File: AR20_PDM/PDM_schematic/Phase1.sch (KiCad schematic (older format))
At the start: 19 parts, among them Q1 BTS50025-1TAD, U1 INA233

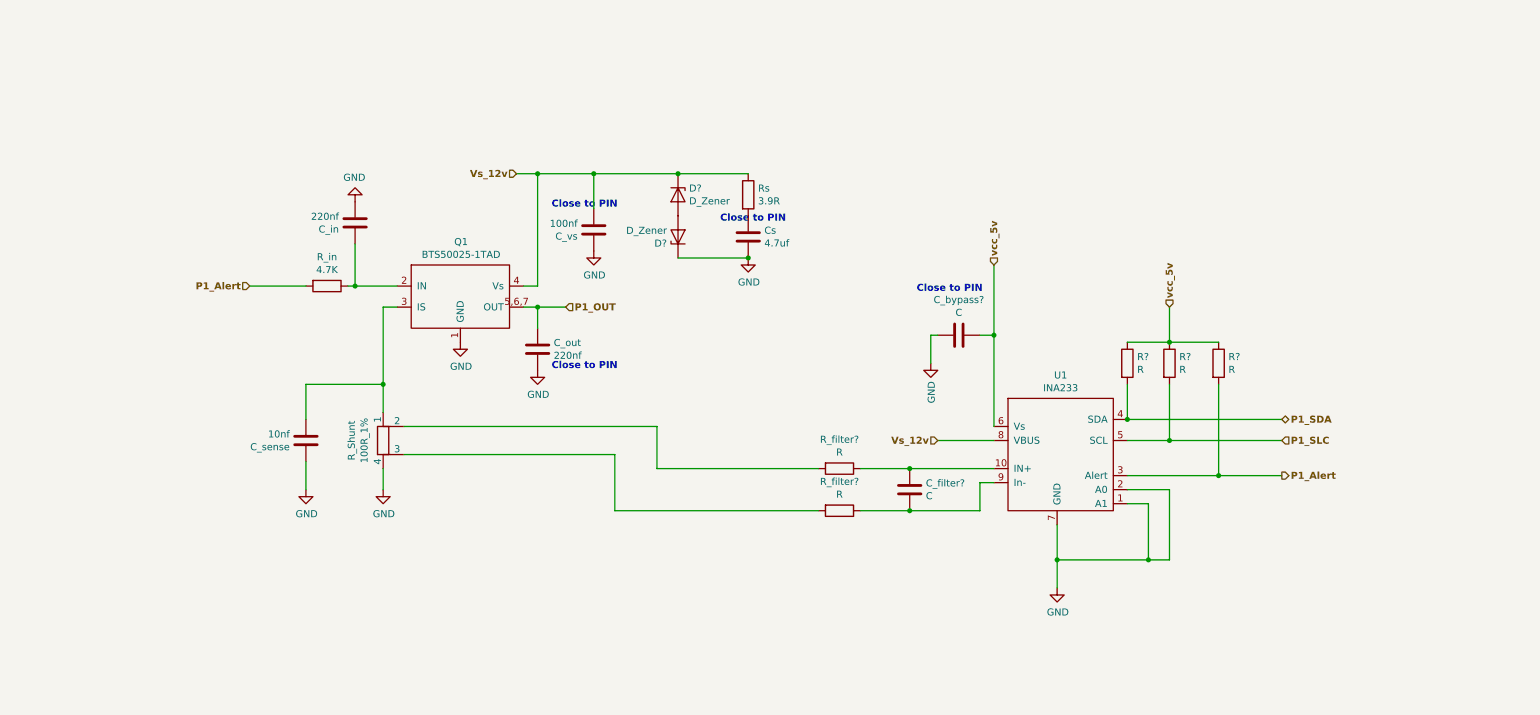
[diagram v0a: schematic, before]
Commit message: Refining pdm schematics
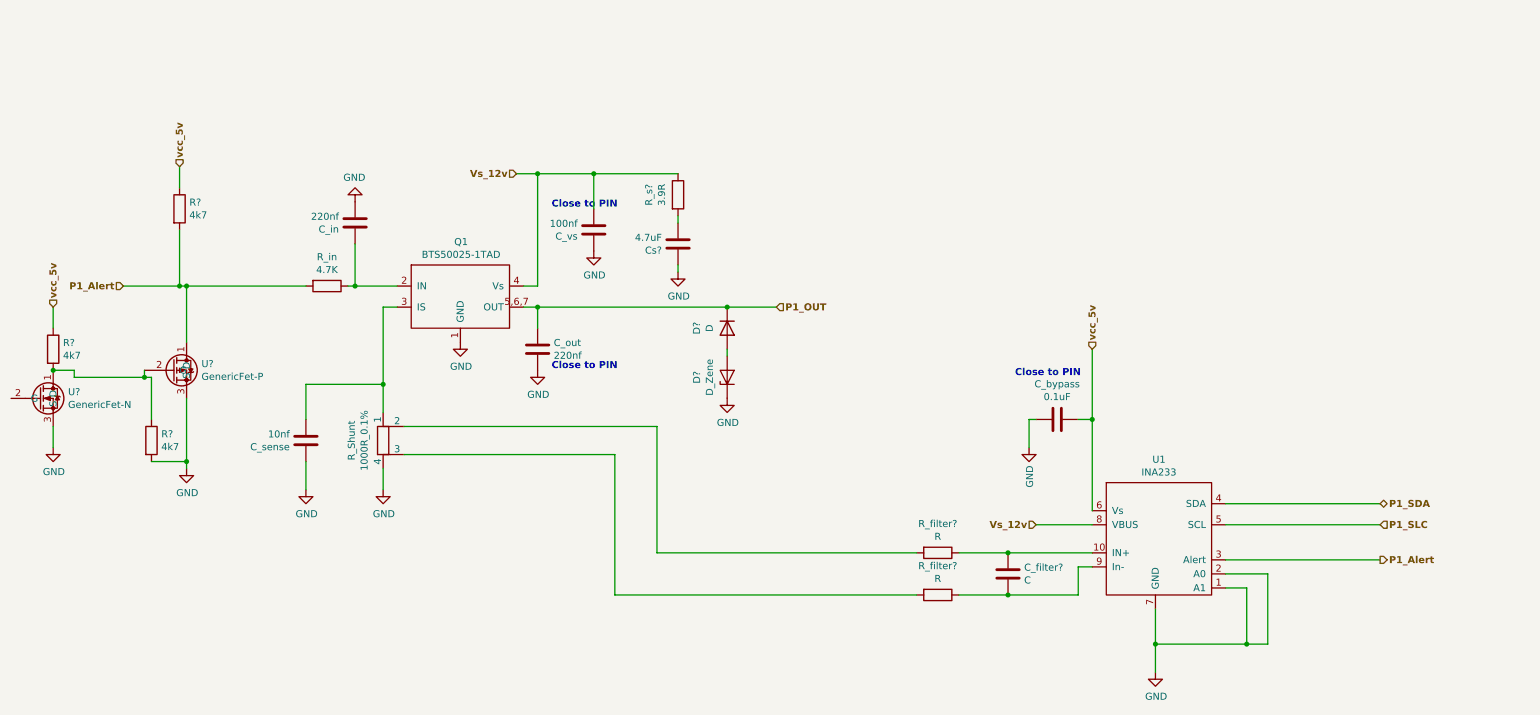
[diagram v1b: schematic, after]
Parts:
- removed Cs: 4.7uf, symbol AR20_PDM_v1-rescue:C-Device
- removed D? (x2): D_Zener, symbol AR20_PDM_v1-rescue:D_Zener-Device
- removed R? (x2): R, symbol AR20_PDM_v1-rescue:R-Device
- removed Rs: 3.9R, symbol AR20_PDM_v1-rescue:R-Device
- added Cs?: 4.7uF, symbol AR20_PDM_v1-rescue:C-Device
- added D?: D_Zene, symbol AR20_PDM_v1-rescue:D_Zener-Device
- added D?: D, symbol AR20_PDM_v1-rescue:DIODE-Simulation_SPICE
- added R? (x2): 4k7, symbol AR20_PDM_v1-rescue:R-Device
- added R_s?: 3.9R, symbol AR20_PDM_v1-rescue:R-Device
- added U?: GenericFet-P, symbol AR20_PDM_v1-rescue:GenericFet-P
- added U?: GenericFet-N, symbol AR20_PDM_v1-rescue:GenericFet-N
- C_bypass: renamed from C_bypass?; value C -> 0.1uF
- R?: value R -> 4k7
- R_Shunt: value 100R_1% -> 1000R_0.1%
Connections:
- net GND: now also Cs?.1, D?.1 (K), R?.2, U?.3 (S), U?.3 (S)
- net P1_Alert: now also U?.1 (D)
- net P1_OUT: now also D?.2 (K)
- net Vs_12v: now also R_s?.1
- net vcc_5v: now also R?.1
- new net: D?.1 (A), D?.2 (A)
- new net: Cs?.2, R_s?.2
- new net: R?.1, R?.2, U?.1 (D), U?.2 (G)
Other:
- moved on the sheet: C_bypass, C_filter?, R?, R_filter?, U1

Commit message: Refining pdm phase 1
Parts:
- removed R?: 4k7, symbol AR20_PDM_v1-rescue:R-Device
- removed U?: GenericFet-P, symbol AR20_PDM_v1-rescue:GenericFet-P
- removed U?: GenericFet-N, symbol AR20_PDM_v1-rescue:GenericFet-N
- added R?: 4k7, symbol AR20_PDM_v1-rescue:R-Device
- added U? (x2): Fet-P, symbol AR20_PDM_v1-rescue:GenericFet-P
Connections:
- net GND: now also R?.2, U?.3 (S), U?.3 (S)
- net P1_Alert: now also U?.1 (D), U?.1 (D)
- net P1_EN: now reaches R?.1
- net P1_EN: now also U?.2 (G)
- new net P1_mcu_EN: R?.1, U?.2 (G)
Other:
- moved on the sheet: C_bypass, C_filter?, C_in, C_out, C_sense, C_vs, Cs?, D?, Q1, R?, R_Shunt, R_filter?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

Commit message: PDM Phase 1 mostly complete
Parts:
- removed C_filter?: C, symbol AR20_PDM_v1-rescue:C-Device
- removed R_filter? (x2): R, symbol AR20_PDM_v1-rescue:R-Device
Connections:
- net at U1.10 (IN+): now also R_Shunt.2
- net at U1.9 (In-): now also R_Shunt.3
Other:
- note added: "Configurable address, \nmust be different for each chip"
- moved on the sheet: R?, U?
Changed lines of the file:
@@
-$EndComp
-$Comp
-L AR20_PDM_v1-rescue:C-Device C_filter?
-U 1 1 5DAAC1F5
-P 8150 4450
-F 0 "C_filter?" H 8265 4496 50  0000 L CNN
-F 1 "C" H 8265 4405 50  0000 L CNN
-F 2 "" H 8188 4300 50  0001 C CNN
-F 3 "~" H 8150 4450 50  0001 C CNN
-	1    8150 4450
-	1    0    0    -1
 $EndComp
 $Comp
@@
 Wire Wire Line
 	4800 2550 4800 2700
-Wire Wire Line
-	9200 4700 9200 4950
-Wire Wire Line
-	8750 4300 8150 4300
-Connection ~ 8150 4300
 $Comp
 L AR20_PDM_v1-rescue:GND-power #PWR?
@@
 	3700 3850 3700 3700
 Wire Wire Line
-	8150 4600 7800 4600
-Wire Wire Line
-	7800 4300 8150 4300
-Wire Wire Line
 	8750 2850 8750 3350
 Wire Wire Line
@@
 Wire Wire Line
 	9700 4450 10000 4450
-Wire Wire Line
-	10000 4450 10000 4950
 $Comp
 L AR20_PDM_v1-rescue:GND-power #PWR?
@@
 Wire Wire Line
 	3500 2400 3800 2400
-Wire Wire Line
-	9850 4950 9200 4950
-Connection ~ 9200 4950
-Wire Wire Line
-	9200 4950 9200 5150
-Wire Wire Line
-	9850 4950 10000 4950
-Connection ~ 9850 4950
 $Comp
 L AR20_PDM_v1-rescue:BTS50025-1TAD Q1
@@
 	3850 3600 5350 3600
 Wire Wire Line
-	3850 3400 5650 3400
+	3850 3400 5450 3400
 Text HLabel 2250 1550 1    50   Input ~ 10
 vcc_5v
-Wire Wire Line
-	8750 4400 8650 4400
-Wire Wire Line
-	8650 4400 8650 4600
-Wire Wire Line
-	8650 4600 8150 4600
-Connection ~ 8150 4600
 Wire Wire Line
 	9700 4100 10350 4100
@@
 Connection ~ 5200 1600
 Wire Wire Line
-	5650 3400 5650 4300
-Wire Wire Line
-	5650 4300 7500 4300
-$Comp
-L AR20_PDM_v1-rescue:R-Device R_filter?
-U 1 1 5DAAC263
-P 7650 4600
-F 0 "R_filter?" V 7443 4600 50  0000 C CNN
-F 1 "R" V 7534 4600 50  0000 C CNN
-F 2 "" V 7580 4600 50  0001 C CNN
-F 3 "~" H 7650 4600 50  0001 C CNN
-	1    7650 4600
-	0    1    1    0
-$EndComp
-$Comp
-L AR20_PDM_v1-rescue:R-Device R_filter?
-U 1 1 5DAAC1FB
-P 7650 4300
-F 0 "R_filter?" V 7443 4300 50  0000 C CNN
-F 1 "R" V 7534 4300 50  0000 C CNN
-F 2 "" V 7580 4300 50  0001 C CNN
-F 3 "~" H 7650 4300 50  0001 C CNN
-	1    7650 4300
-	0    1    1    0
-$EndComp
-Wire Wire Line
-	7500 4600 5350 4600
-Wire Wire Line
-	5350 3600 5350 4600
-Text HLabel 1250 1900 1    50   Input ~ 10
+	5450 3400 5450 4300
+Wire Wire Line
+	5350 3600 5350 4400
+Text HLabel 1350 1900 1    50   Input ~ 10
 P1_Alert
 Wire Wire Line
@@
 $Comp
 L AR20_PDM_v1-rescue:GND-power #PWR?
-U 1 1 5DC19763
-P 2500 3600
-F 0 "#PWR?" H 2500 3350 50  0001 C CNN
-F 1 "GND" H 2505 3427 50  0000 C CNN
-F 2 "" H 2500 3600 50  0001 C CNN
-F 3 "" H 2500 3600 50  0001 C CNN
-	1    2500 3600
-	1    0    0    -1
-$EndComp
-Wire Wire Line
-	2500 3200 2500 3550
-Connection ~ 2500 3550
-Wire Wire Line
-	2500 3550 2500 3600
+U 1 1 5DC2BC32
+P 1350 3600
+F 0 "#PWR?" H 1350 3350 50  0001 C CNN
+F 1 "GND" H 1355 3427 50  0000 C CNN
+F 2 "" H 1350 3600 50  0001 C CNN
+F 3 "" H 1350 3600 50  0001 C CNN
+	1    1350 3600
+	1    0    0    -1
+$EndComp
+Wire Wire Line
+	1350 3200 1350 3550
+Wire Wire Line
+	1000 3550 1350 3550
+Connection ~ 1350 3550
+Wire Wire Line
+	1350 3550 1350 3600
+Wire Wire Line
+	1350 2400 1350 2800
+$Comp
+L AR20_PDM_v1-rescue:R-Device R?
+U 1 1 5DC2BC49
+P 1000 3400
+F 0 "R?" H 1070 3446 50  0000 L CNN
+F 1 "4k7" H 1070 3355 50  0000 L CNN
+F 2 "" V 930 3400 50  0001 C CNN
+F 3 "~" H 1000 3400 50  0001 C CNN
+	1    1000 3400
+	1    0    0    -1
+$EndComp
+Wire Wire Line
+	1000 3250 1000 3000
+Wire Wire Line
+	1000 3000 1050 3000
+Wire Wire Line
+	1350 1900 1350 2400
+Connection ~ 1350 2400
+Wire Wire Line
+	1350 2400 2250 2400
+Wire Wire Line
+	2250 2400 2500 2400
+Connection ~ 2500 2400
+Wire Wire Line
+	2500 2400 3150 2400
+$Comp
+L AR20_PDM_v1-rescue:GenericFet-P U?
+U 1 1 5DC2BC43
+P 1350 2500
+F 0 "U?" H 1456 2046 50  0000 L CNN
+F 1 "Fet-P" H 1456 1955 50  0000 L CNN
+F 2 "" H 1350 2500 50  0001 C CNN
+F 3 "" H 1350 2500 50  0001 C CNN
+	1    1350 2500
+	1    0    0    -1
+$EndComp
+Connection ~ 1000 3000
+Text HLabel 700  3100 3    50   Input ~ 0
+P1_mcu_EN
+Wire Wire Line
+	700  3000 700  3100
+Wire Wire Line
+	700  3000 1000 3000
+Wire Wire Line
+	5450 4300 8750 4300
+Wire Wire Line
+	5350 4400 8750 4400
+Wire Wire Line
+	9200 4950 9200 5150
+Wire Wire Line
+	9200 4700 9200 4950
+Connection ~ 9200 4950
+Wire Wire Line
+	9850 4950 9200 4950
+Connection ~ 9850 4950
+Wire Wire Line
+	9850 4950 10000 4950
+Wire Wire Line
+	10000 4450 10000 4950
+Text Notes 9650 4750 0    50   ~ 10
+Configurable address, \nmust be different for each chip
+Wire Wire Line
+	1850 3000 2150 3000
+Wire Wire Line
+	1850 3100 1850 3000
+Text HLabel 1850 3100 3    50   Input ~ 0
+P1_EN
+Connection ~ 2150 3000
+Wire Wire Line
+	2150 3550 2500 3550
+Wire Wire Line
+	2150 3450 2150 3550
+Wire Wire Line
+	2150 3000 2150 3150
+Wire Wire Line
+	2150 3000 2200 3000
+$Comp
+L AR20_PDM_v1-rescue:R-Device R?
+U 1 1 5DC1F6FA
+P 2150 3300
+F 0 "R?" H 2220 3346 50  0000 L CNN
+F 1 "4k7" H 2220 3255 50  0000 L CNN
+F 2 "" V 2080 3300 50  0001 C CNN
+F 3 "~" H 2150 3300 50  0001 C CNN
+	1    2150 3300
+	1    0    0    -1
+$EndComp
+Wire Wire Line
+	2500 2800 2500 2400
 $Comp
 L AR20_PDM_v1-rescue:GenericFet-P U?
@@
 	1    0    0    -1
 $EndComp
-$Comp
-L AR20_PDM_v1-rescue:GND-power #PWR?
-U 1 1 5DC2BC32
-P 1250 3600
-F 0 "#PWR?" H 1250 3350 50  0001 C CNN
-F 1 "GND" H 1255 3427 50  0000 C CNN
-F 2 "" H 1250 3600 50  0001 C CNN
-F 3 "" H 1250 3600 50  0001 C CNN
-	1    1250 3600
-	1    0    0    -1
-$EndComp
-Wire Wire Line
-	1250 3200 1250 3550
-Wire Wire Line
-	900  3550 1250 3550
-Connection ~ 1250 3550
-Wire Wire Line
-	1250 3550 1250 3600
-Wire Wire Line
-	1250 2400 1250 2800
-$Comp
-L AR20_PDM_v1-rescue:R-Device R?
-U 1 1 5DC2BC49
-P 900 3400
-F 0 "R?" H 970 3446 50  0000 L CNN
-F 1 "4k7" H 970 3355 50  0000 L CNN
-F 2 "" V 830 3400 50  0001 C CNN
-F 3 "~" H 900 3400 50  0001 C CNN
-	1    900  3400
-	1    0    0    -1
-$EndComp
-Wire Wire Line
-	900  3250 900  3000
-Wire Wire Line
-	900  3000 950  3000
-Wire Wire Line
-	1250 1900 1250 2400
-Connection ~ 1250 2400
-Wire Wire Line
-	1250 2400 2250 2400
-Wire Wire Line
-	2500 2800 2500 2400
-Wire Wire Line
-	2250 2400 2500 2400
-Connection ~ 2500 2400
-Wire Wire Line
-	2500 2400 3150 2400
-$Comp
-L AR20_PDM_v1-rescue:R-Device R?
-U 1 1 5DC1F6FA
-P 2150 3300
-F 0 "R?" H 2220 3346 50  0000 L CNN
-F 1 "4k7" H 2220 3255 50  0000 L CNN
-F 2 "" V 2080 3300 50  0001 C CNN
-F 3 "~" H 2150 3300 50  0001 C CNN
-	1    2150 3300
-	1    0    0    -1
-$EndComp
-Wire Wire Line
-	2150 3000 2200 3000
-Wire Wire Line
-	2150 3000 2150 3150
-Wire Wire Line
-	2150 3450 2150 3550
-Wire Wire Line
-	2150 3550 2500 3550
-$Comp
-L AR20_PDM_v1-rescue:GenericFet-P U?
-U 1 1 5DC2BC43
-P 1250 2500
-F 0 "U?" H 1356 2046 50  0000 L CNN
-F 1 "Fet-P" H 1356 1955 50  0000 L CNN
-F 2 "" H 1250 2500 50  0001 C CNN
-F 3 "" H 1250 2500 50  0001 C CNN
-	1    1250 2500
-	1    0    0    -1
-$EndComp
-Connection ~ 900  3000
-Connection ~ 2150 3000
-Text HLabel 1850 3100 3    50   Input ~ 0
-P1_EN
-Wire Wire Line
-	1850 3100 1850 3000
-Wire Wire Line
-	1850 3000 2150 3000
-Text HLabel 600  3100 3    50   Input ~ 0
-P1_mcu_EN
-Wire Wire Line
-	600  3000 600  3100
-Wire Wire Line
-	600  3000 900  3000
+Wire Wire Line
+	2500 3550 2500 3600
+Connection ~ 2500 3550
+Wire Wire Line
+	2500 3200 2500 3550
+$Comp
+L AR20_PDM_v1-rescue:GND-power #PWR?
+U 1 1 5DC19763
+P 2500 3600
+F 0 "#PWR?" H 2500 3350 50  0001 C CNN
+F 1 "GND" H 2505 3427 50  0000 C CNN
+F 2 "" H 2500 3600 50  0001 C CNN
+F 3 "" H 2500 3600 50  0001 C CNN
+	1    2500 3600
+	1    0    0    -1
+$EndComp
 $EndSCHEMATC

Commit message: PDM: VOL1 + Breakout board
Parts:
- Q1: footprint (none) -> PDM_footprint:BTS50055-1TMA
- U1: footprint (none) -> PDM_footprint:INA233
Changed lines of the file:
@@
 F 0 "Q1" H 4255 3215 50  0000 C CNN
 F 1 "BTS50025-1TAD" H 4255 3124 50  0000 C CNN
-F 2 "" H 4250 2650 50  0001 C CNN
+F 2 "PDM_footprint:BTS50055-1TMA" H 4250 2650 50  0001 C CNN
 F 3 "" H 4250 2650 50  0001 C CNN
 	1    4250 2650
@@
 F 0 "U1" H 9225 4465 50  0000 C CNN
 F 1 "INA233" H 9225 4374 50  0000 C CNN
-F 2 "" H 9200 4050 50  0001 C CNN
+F 2 "PDM_footprint:INA233" H 9200 4050 50  0001 C CNN
 F 3 "" H 9200 4050 50  0001 C CNN
 	1    9200 4050
